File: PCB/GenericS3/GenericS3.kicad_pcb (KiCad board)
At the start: 2 copper layers, 70 x 70 mm, 73 parts, among them J1 USB-C, J2 Shelly, J3 POWER, P1 33, P10 42, P11 45, P12 46, P13 47, P14 48, P15 18, P16 19, P17 14, P18 15, P19 16, P2 34, P20 17, P21 6, P22 7, P23 8, P24 9, P25 20, P26 10, P27 11, P28 12, P29 13, P3 35, P30 1, P31 2, P32 3, P33 4, P34 5, P35 21, P36 43, P37 44, P38 0, P39 ⏚, P4 36, P40 ⏚, P41 ⏚, P42 ⏚, P43 +, P44 +, P45 +, P46 +, P5 37, P6 38, P7 39, P8 40, P9 41, SW1 SW_Push, SW2 SW_Push, U1 Barcode, U2 ESP32-S3-MINI-1, U5 MD8942

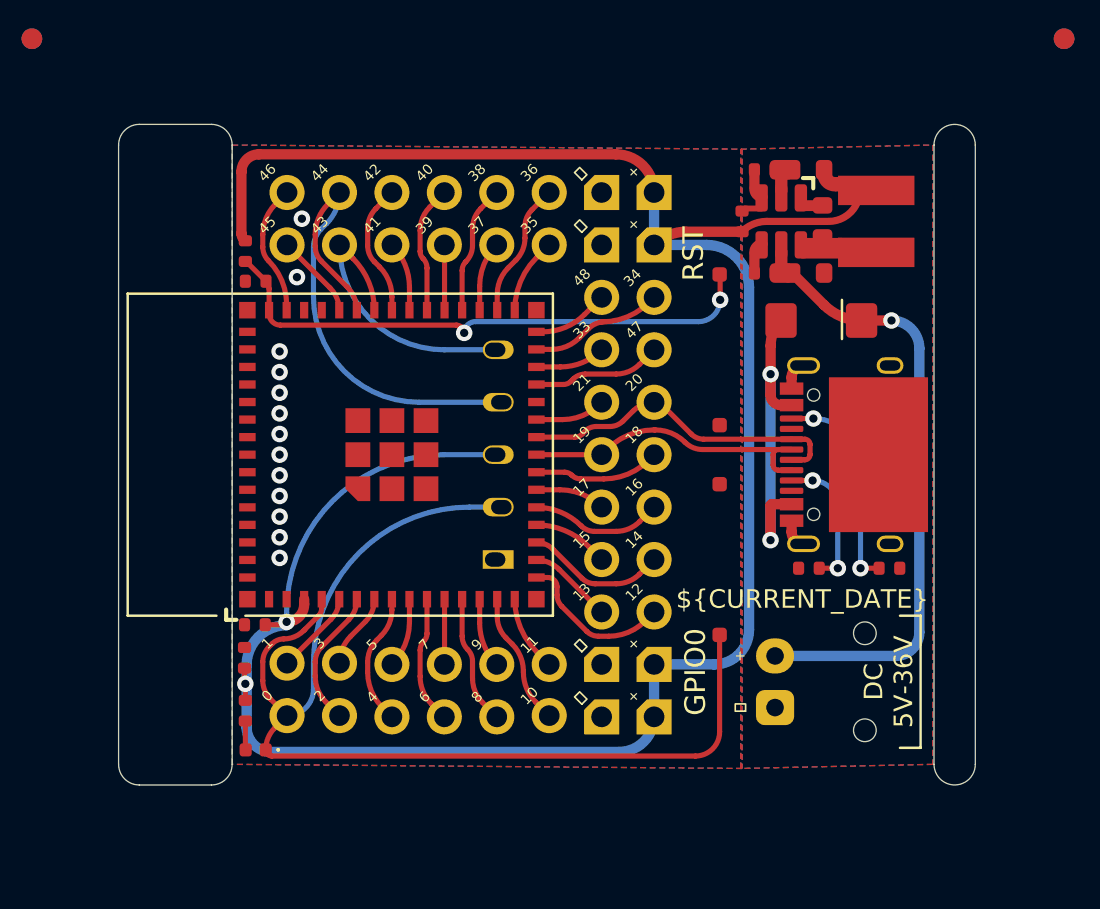
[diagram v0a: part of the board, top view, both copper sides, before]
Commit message: No buttons
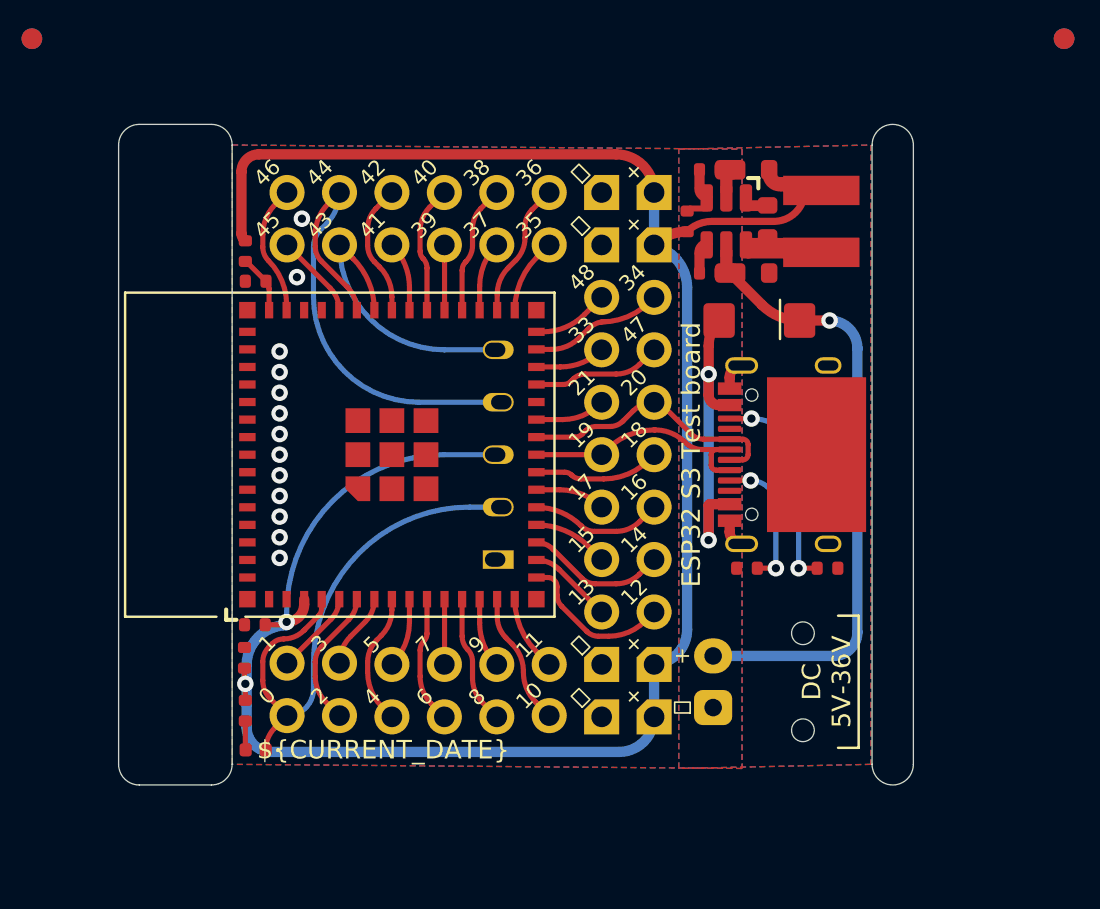
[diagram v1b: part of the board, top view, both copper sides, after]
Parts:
- removed SW1, SW2: SW_Push, RevK:TS-1092S-B3D2-G
- moved D1 3.00 mm to (110.2, 82.5)
- moved J1 3.00 mm to (111.3, 89.0)
- moved J3 3.00 mm to (108.0, 100.0)
- moved R2 3.00 mm to (109.6, 94.5)
- moved R3 3.00 mm to (113.5, 94.5)
- moved L2 2.66 mm to (113.2, 77.7)
- moved R9 2.66 mm to (106.7, 77.7)
- moved C6 2.66 mm to (109.9, 80.2)
- moved C7 2.66 mm to (109.9, 75.2)
- moved C8 2.66 mm to (110.6, 77.7)
- moved R10 2.66 mm to (107.8, 75.2)
- moved R11 2.66 mm to (107.8, 80.2)
- moved U5 2.66 mm to (108.6, 77.7)
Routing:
- net Net-(D2-K): track 53.4 -> 25.9 mm
- net Net-(U2-EN): track 27.2 -> 2.76 mm, vias 2 -> 0
- net +3.3V: track 108.2 -> 100.0 mm
- net D-: track 15.1 -> 12.1 mm
- net D+: track 15.6 -> 12.6 mm
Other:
- board text removed: "GPIO0"
- board text removed: "RST"

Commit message: Tweak
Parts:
- moved C1 1.00 mm to (86.8, 97.2)
- moved C2 1.00 mm to (86.3, 98.8)
- moved C3 1.00 mm to (86.8, 80.6)
- moved C6 1.00 mm to (110.9, 80.2)
- moved C7 1.00 mm to (110.9, 75.2)
- moved C8 1.00 mm to (111.6, 77.7)
- moved D1 1.00 mm to (111.2, 82.5)
- moved D2 1.00 mm to (86.8, 103.3)
- moved J1 1.00 mm to (112.3, 89.0)
- moved J2 1.00 mm to (98.6, 89.0)
- moved J3 1.00 mm to (109.0, 100.0)
- moved L2 1.00 mm to (114.2, 77.7)
- moved P1 1.00 mm to (103.6, 83.9)
- moved P10 1.00 mm to (93.4, 76.3)
- moved P11 1.00 mm to (88.4, 78.8)
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
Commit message: Silk
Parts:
- moved D1 0.70 mm to (111.9, 82.5)
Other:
- board text removed: "DC 5V USB"

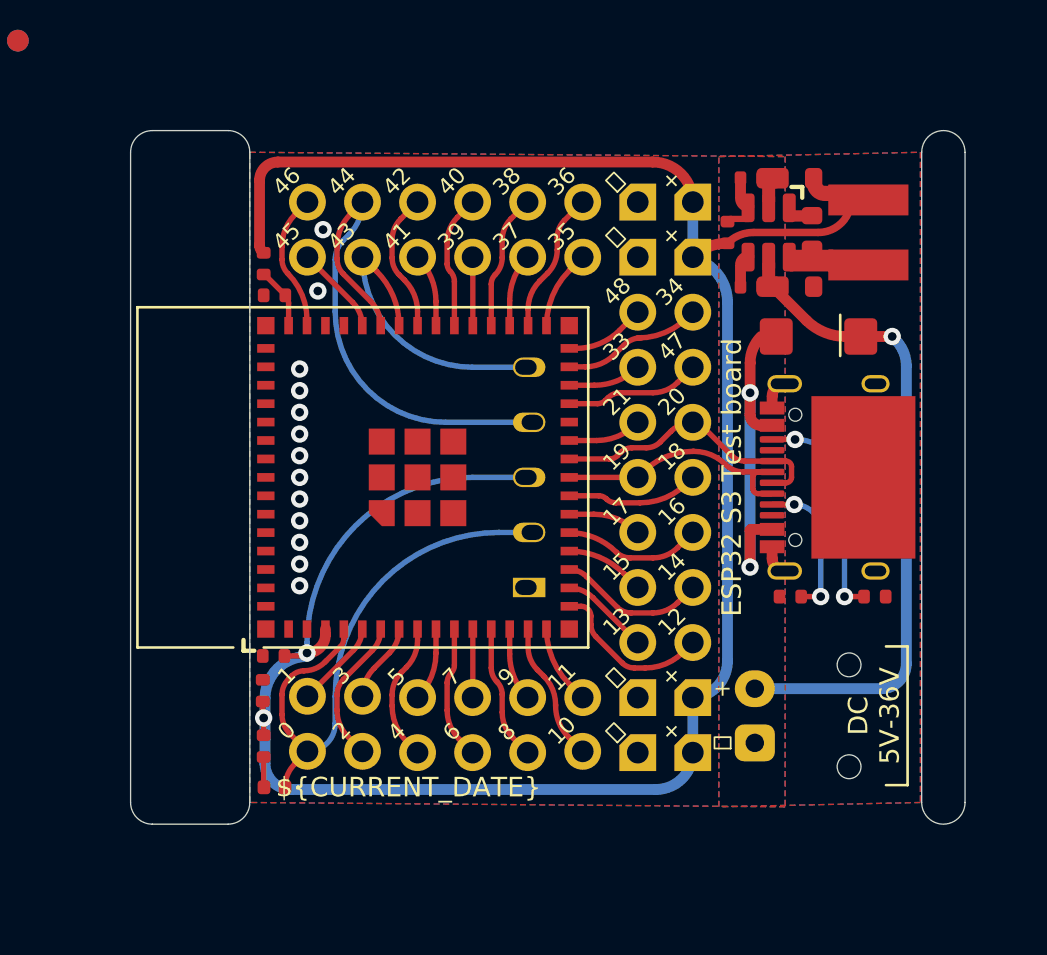
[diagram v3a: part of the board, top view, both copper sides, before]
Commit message: Packed in to 30x30mm
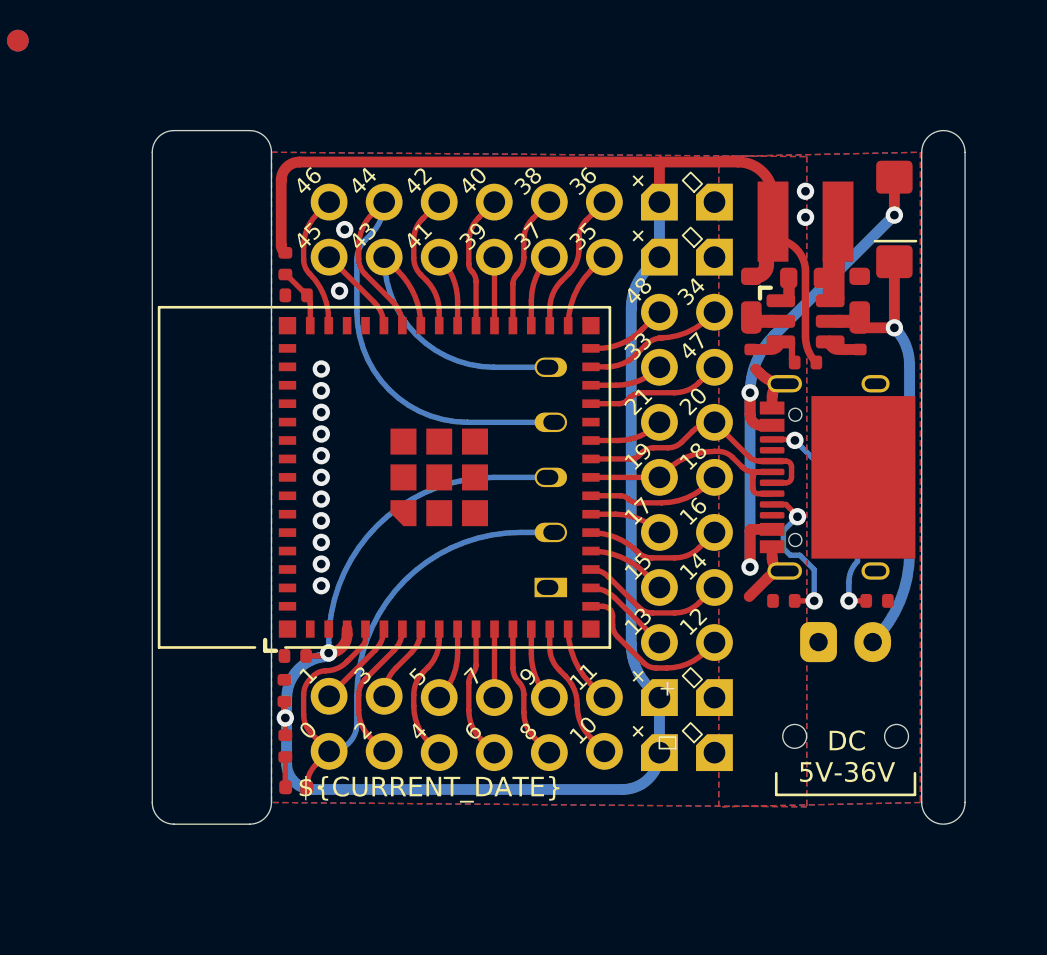
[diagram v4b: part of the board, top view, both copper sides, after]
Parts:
- moved R10 7.40 mm to (108.8, 82.6), turned to 90 degrees
- moved R9 7.00 mm to (111.3, 83.7), turned to 180 degrees
- moved D1 6.44 mm to (115.4, 77.1), turned to 90 degrees
- moved C7 5.70 mm to (108.8, 80.5), turned to -90 degrees
- moved R11 5.55 mm to (113.8, 82.6), turned to -90 degrees
- moved J3 5.40 mm to (113.2, 96.6), turned to 0 degrees
- moved U5 4.44 mm to (111.3, 81.8), turned to 180 degrees
- moved P39 3.54 mm to (107.1, 99.2)
- moved P40 3.54 mm to (107.1, 101.7)
- moved P41 3.54 mm to (107.1, 76.3)
- moved P42 3.54 mm to (107.1, 78.8)
- moved L2 2.94 mm to (111.3, 77.2), turned to 180 degrees
- moved C6 2.92 mm to (113.8, 80.5), turned to -90 degrees
- moved C8 2.12 mm to (111.3, 79.8), turned to 180 degrees
- moved P43 1.54 mm to (104.6, 76.3)
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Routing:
- net Net-(D1-A): track 15.8 -> 25.6 mm, vias 2 -> 3
- net DC: track 29.2 -> 19.8 mm
- net GND: track 2.86 -> 6.48 mm, vias 13 -> 15
- net +3.3V: track 100.0 -> 98.2 mm
- net D-: track 12.1 -> 11.2 mm
- net Net-(P28-P): track 7.65 -> 7.01 mm
- net Net-(J1-CC1): track 6.82 -> 7.32 mm

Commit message: Tidy
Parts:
- moved D1 0.14 mm to (115.3, 77.0)
- moved C6 0.10 mm to (113.7, 80.5)
- moved C7 0.10 mm to (108.7, 80.5)
- moved C8 0.10 mm to (111.2, 79.8)
- moved L2 0.10 mm to (111.2, 77.2)
- moved R10 0.10 mm to (108.7, 82.6)
- moved R11 0.10 mm to (113.7, 82.6)
- moved R9 0.10 mm to (111.2, 83.7)
- moved U5 0.10 mm to (111.2, 81.8)
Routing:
- net GND: track 6.48 -> 11.4 mm, vias 15 -> 17
- net Net-(J1-CC1): track 7.32 -> 6.82 mm

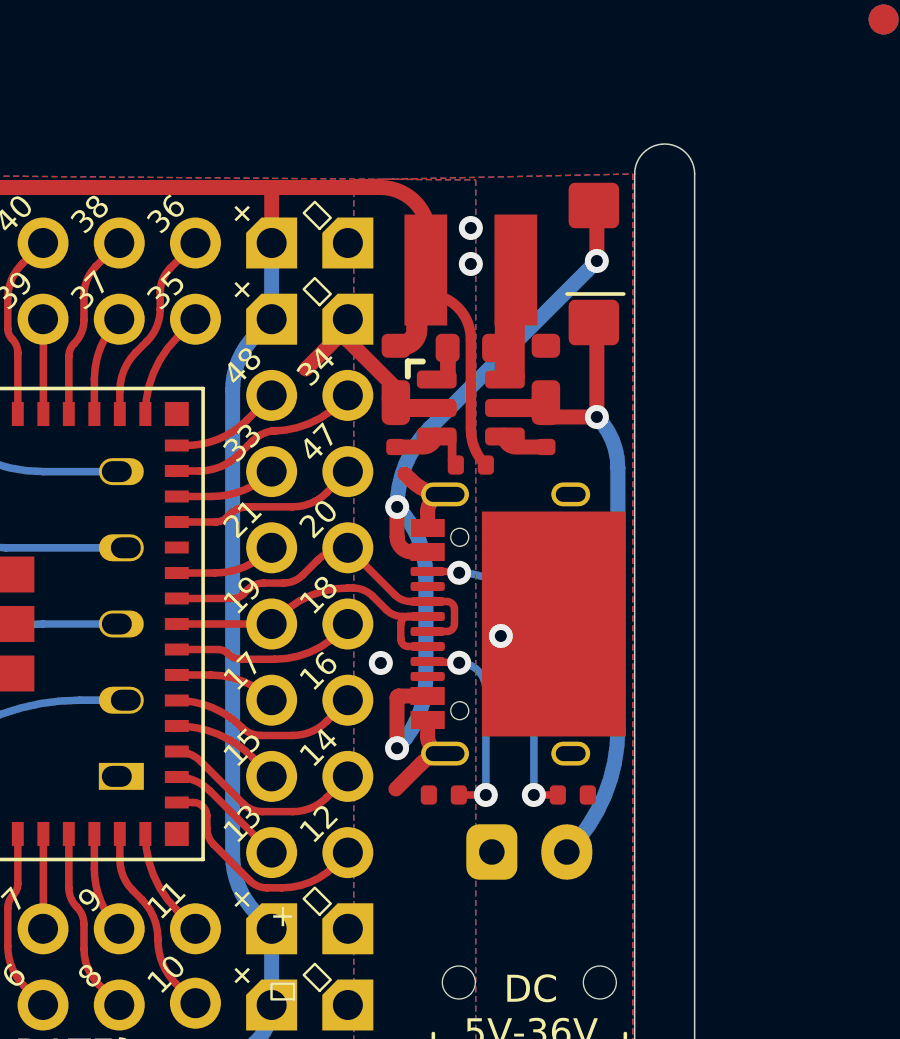
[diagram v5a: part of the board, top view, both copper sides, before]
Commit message: Smaller diode
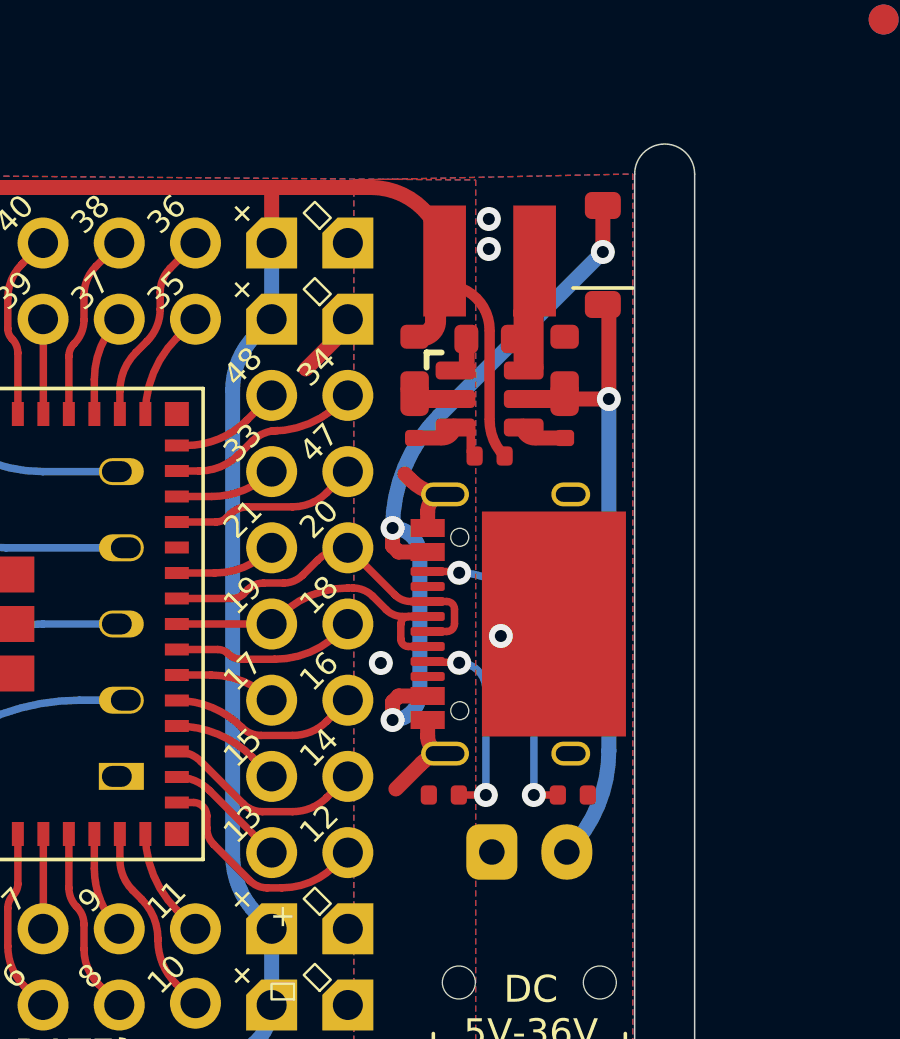
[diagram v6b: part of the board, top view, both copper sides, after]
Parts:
- D1: footprint RevK:D_SMA -> RevK:D_SOD-123
- moved C6 0.69 mm to (114.4, 80.2)
- moved C7 0.69 mm to (109.4, 80.2)
- moved C8 0.69 mm to (111.9, 79.5)
- moved L2 0.69 mm to (111.9, 76.9)
- moved R10 0.69 mm to (109.4, 82.3)
- moved R11 0.69 mm to (114.4, 82.3)
- moved R9 0.69 mm to (111.9, 83.4)
- moved U5 0.69 mm to (111.9, 81.5)
- moved D1 0.42 mm to (115.6, 76.7)
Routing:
- net GND: track 11.4 -> 8.46 mm
- net Net-(D1-A): track 26.1 -> 24.5 mm
- net +3.3V: track 98.2 -> 99.2 mm

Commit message: No barcode
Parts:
- removed U1: Barcode, RevK:EAN-5060634238120
- moved C1 10.0 mm to (87.8, 107.2)
- moved C2 10.0 mm to (87.3, 108.8)
- moved C3 10.0 mm to (87.8, 90.6)
- moved C6 10.0 mm to (114.4, 90.2)
- moved C7 10.0 mm to (109.4, 90.2)
- moved C8 10.0 mm to (111.9, 89.5)
- moved D1 10.0 mm to (115.6, 86.7)
- moved D2 10.0 mm to (87.8, 113.3)
- moved J1 10.0 mm to (112.3, 99.0)
- moved J2 10.0 mm to (99.6, 99.0)
- moved J3 10.0 mm to (113.2, 106.6)
- moved L2 10.0 mm to (111.9, 86.9)
- moved P1 10.0 mm to (104.6, 93.9)
- moved P10 10.0 mm to (94.4, 86.3)
- moved P11 10.0 mm to (89.4, 88.8)
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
